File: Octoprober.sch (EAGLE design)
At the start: 98 parts, among them J1 10118193-0001LF, P1 TC33X-1, SW1 EVQ-Q2203W, SW2 EVQ-Q2203W, SW3 EVQ-Q2203W, SW4 EVQ-Q2203W, SW5 EVQ-Q2203W, U1 P8X32A-M44, U10 MAX31855KASA+, U11 MAX31855KASA+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

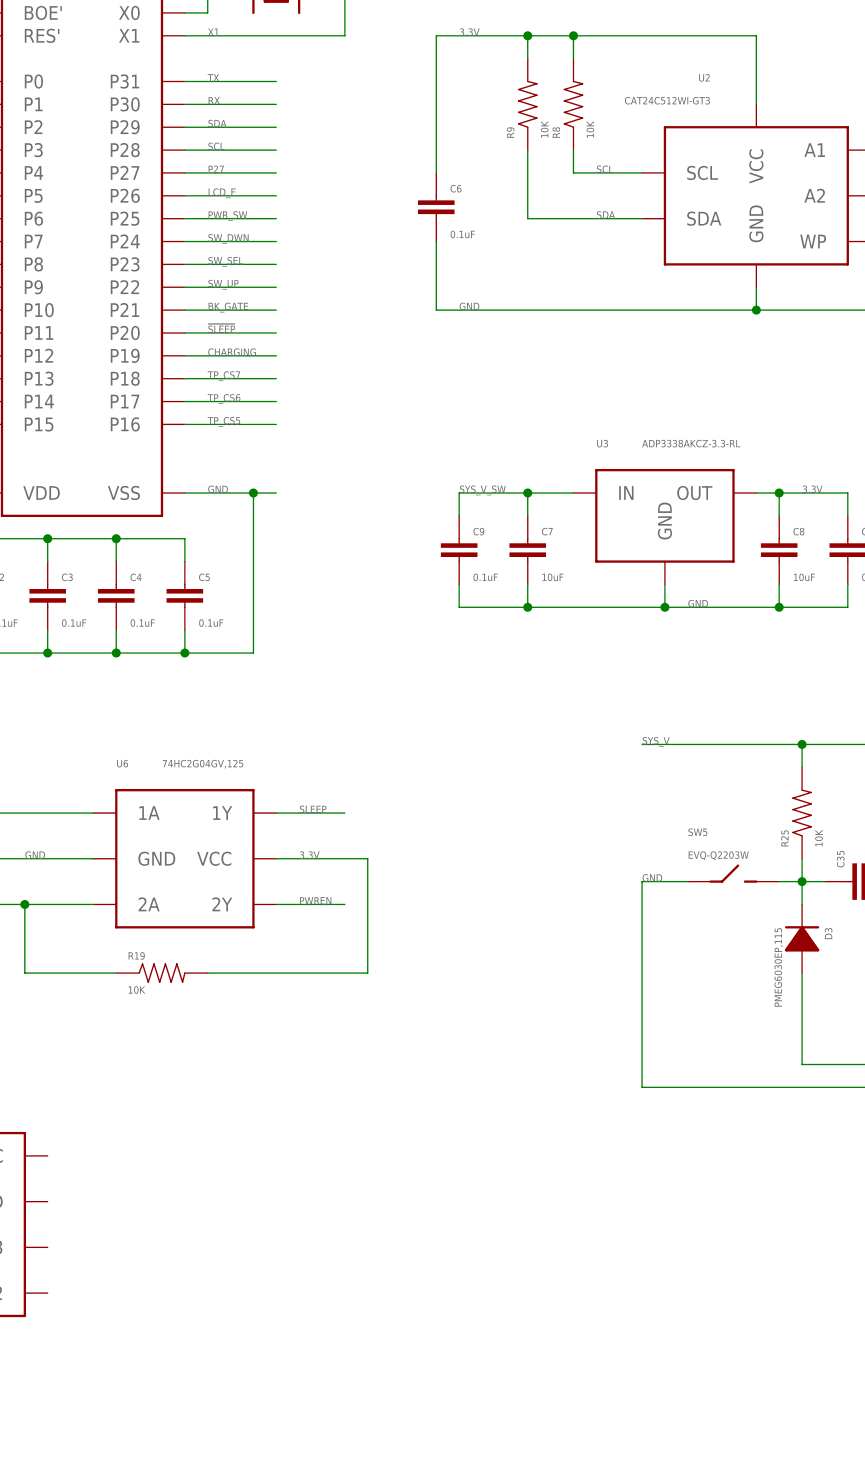
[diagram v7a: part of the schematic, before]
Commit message: Add optocouple.
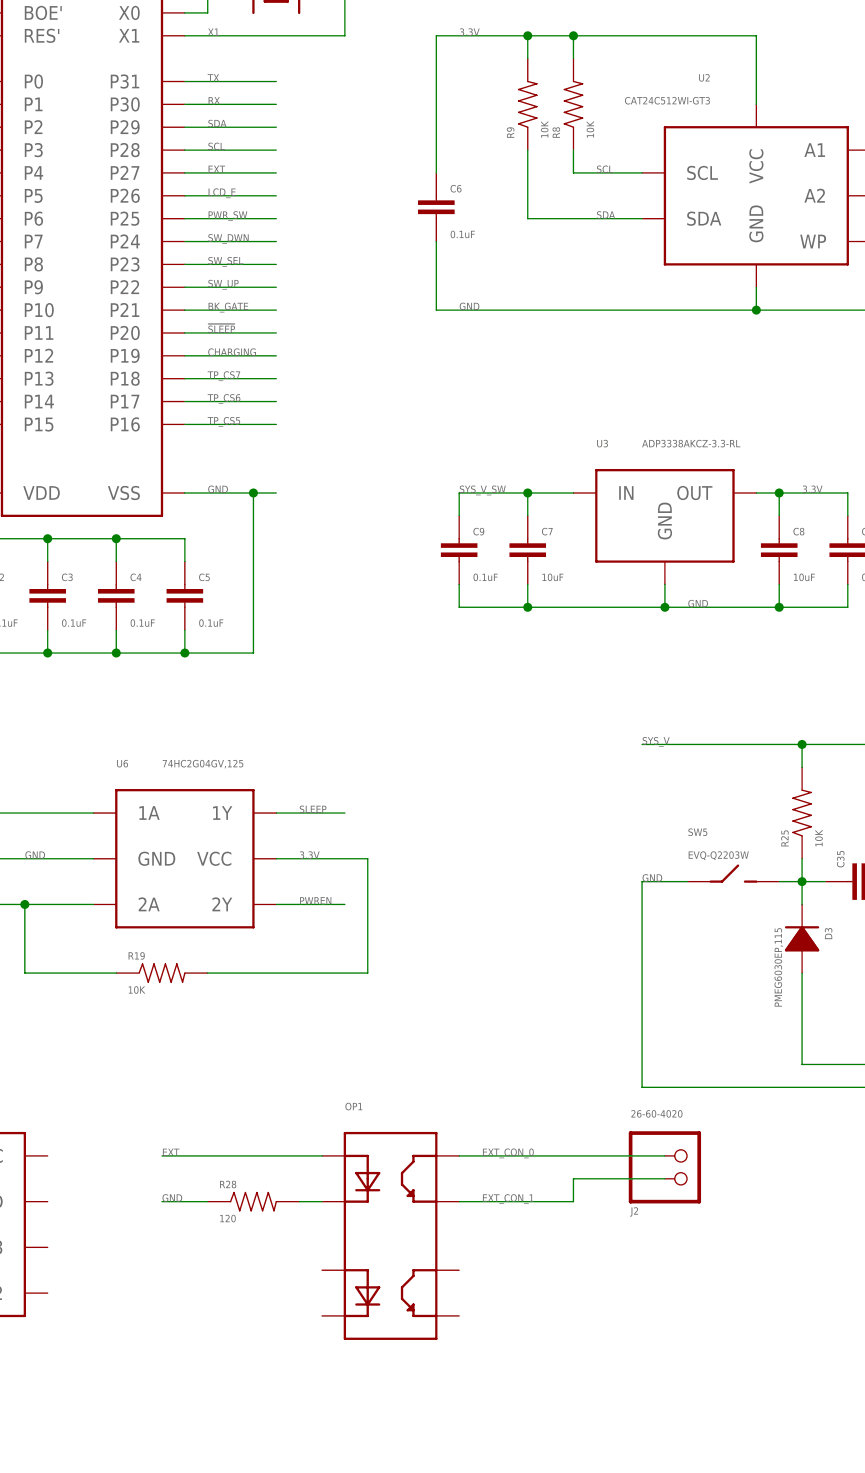
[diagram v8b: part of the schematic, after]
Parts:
- added J2: 26-60-4020, PP_Connectors:PH_1X02MOLEX_26-61-4020
- added OP1: (no value), PP_DigitalIC:ACPL-227SOIC-8
- added R28: 120, PP_Passives:RESISTOR0402
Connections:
- removed net P27: U1.P27
- new net EXT: OP1.1, U1.P27
- new net EXT_CON_0: J2.2, OP1.8
- new net EXT_CON_1: J2.1, OP1.7
- new net N$6: OP1.2, R28.2
- net GND: now also R28.1
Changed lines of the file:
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@@
 <?xml version="1.0" encoding="utf-8"?>
 <!DOCTYPE eagle SYSTEM "eagle.dtd">
-<eagle version="6.3">
+<eagle version="6.5.0">
 <drawing>
 <settings>
@@
 <grid distance="0.1" unitdist="inch" unit="inch" style="lines" multiple="1" display="no" altdistance="0.01" altunitdist="inch" altunit="inch"/>
 <layers>
-<layer number="1" name="Top" color="4" fill="1" visible="yes" active="no"/>
-<layer number="16" name="Bottom" color="1" fill="1" visible="yes" active="no"/>
-<layer number="17" name="Pads" color="2" fill="1" visible="yes" active="no"/>
-<layer number="18" name="Vias" color="2" fill="1" visible="yes" active="no"/>
-<layer number="19" name="Unrouted" color="6" fill="1" visible="yes" active="no"/>
-<layer number="20" name="Dimension" color="15" fill="1" visible="yes" active="no"/>
-<layer number="21" name="tPlace" color="7" fill="1" visible="yes" active="no"/>
-<layer number="22" name="bPlace" color="7" fill="1" visible="yes" active="no"/>
-<layer number="23" name="tOrigins" color="15" fill="1" visible="yes" active="no"/>
-<layer number="24" name="bOrigins" color="15" fill="1" visible="yes" active="no"/>
-<layer number="25" name="tNames" color="7" fill="1" visible="yes" active="no"/>
-<layer number="26" name="bNames" color="7" fill="1" visible="yes" active="no"/>
-<layer number="27" name="tValues" color="7" fill="1" visible="yes" active="no"/>
-<layer number="28" name="bValues" color="7" fill="1" visible="yes" active="no"/>
+<layer number="1" name="Top" color="4" fill="1" visible="no" active="no"/>
+<layer number="16" name="Bottom" color="1" fill="1" visible="no" active="no"/>
+<layer number="17" name="Pads" color="2" fill="1" visible="no" active="no"/>
+<layer number="18" name="Vias" color="2" fill="1" visible="no" active="no"/>
+<layer number="19" name="Unrouted" color="6" fill="1" visible="no" active="no"/>
+<layer number="20" name="Dimension" color="15" fill="1" visible="no" active="no"/>
+<layer number="21" name="tPlace" color="7" fill="1" visible="no" active="no"/>
+<layer number="22" name="bPlace" color="7" fill="1" visible="no" active="no"/>
+<layer number="23" name="tOrigins" color="15" fill="1" visible="no" active="no"/>
+<layer number="24" name="bOrigins" color="15" fill="1" visible="no" active="no"/>
+<layer number="25" name="tNames" color="7" fill="1" visible="no" active="no"/>
+<layer number="26" name="bNames" color="7" fill="1" visible="no" active="no"/>
+<layer number="27" name="tValues" color="7" fill="1" visible="no" active="no"/>
+<layer number="28" name="bValues" color="7" fill="1" visible="no" active="no"/>
 <layer number="29" name="tStop" color="7" fill="3" visible="no" active="no"/>
 <layer number="30" name="bStop" color="7" fill="6" visible="no" active="no"/>
@@
 <layer number="35" name="tGlue" color="7" fill="4" visible="no" active="no"/>
 <layer number="36" name="bGlue" color="7" fill="5" visible="no" active="no"/>
-<layer number="37" name="tTest" color="7" fill="1" visible="yes" active="no"/>
-<layer number="38" name="bTest" color="7" fill="1" visible="yes" active="no"/>
+<layer number="37" name="tTest" color="7" fill="1" visible="no" active="no"/>
+<layer number="38" name="bTest" color="7" fill="1" visible="no" active="no"/>
 <layer number="39" name="tKeepout" color="4" fill="11" visible="no" active="no"/>
 <layer number="40" name="bKeepout" color="1" fill="11" visible="no" active="no"/>
@@
 <layer number="44" name="Drills" color="7" fill="1" visible="no" active="no"/>
 <layer number="45" name="Holes" color="7" fill="1" visible="no" active="no"/>
-<layer number="46" name="Milling" color="3" fill="1" visible="yes" active="no"/>
-<layer number="47" name="Measures" color="7" fill="1" visible="yes" active="no"/>
-<layer number="48" name="Document" color="7" fill="1" visible="yes" active="no"/>
-<layer number="49" name="Reference" color="7" fill="1" visible="yes" active="no"/>
-<layer number="50" name="dxf" color="7" fill="1" visible="yes" active="no"/>
-<layer number="51" name="tDocu" color="7" fill="1" visible="yes" active="no"/>
-<layer number="52" name="bDocu" color="7" fill="1" visible="yes" active="no"/>
-<layer number="53" name="tGND_GNDA" color="7" fill="9" visible="yes" active="no"/>
-<layer number="54" name="bGND_GNDA" color="1" fill="9" visible="yes" active="no"/>
-<layer number="56" name="wert" color="7" fill="1" visible="yes" active="no"/>
+<layer number="46" name="Milling" color="3" fill="1" visible="no" active="no"/>
+<layer number="47" name="Measures" color="7" fill="1" visible="no" active="no"/>
+<layer number="48" name="Document" color="7" fill="1" visible="no" active="no"/>
+<layer number="49" name="Reference" color="7" fill="1" visible="no" active="no"/>
+<layer number="50" name="dxf" color="7" fill="1" visible="no" active="no"/>
+<layer number="51" name="tDocu" color="7" fill="1" visible="no" active="no"/>
+<layer number="52" name="bDocu" color="7" fill="1" visible="no" active="no"/>
+<layer number="53" name="tGND_GNDA" color="7" fill="9" visible="no" active="no"/>
+<layer number="54" name="bGND_GNDA" color="1" fill="9" visible="no" active="no"/>
+<layer number="56" name="wert" color="7" fill="1" visible="no" active="no"/>
 <layer number="91" name="Nets" color="2" fill="1" visible="yes" active="yes"/>
 <layer number="92" name="Busses" color="1" fill="1" visible="yes" active="yes"/>
@@
 <part name="U18" library="PP_DigitalIC" deviceset="AD799X" device="SOT-23-8" value="AD7999YRJZ-1500RL7"/>
 <part name="U$2" library="PP_Aesthetics" deviceset="OCTOPROBER_LOGO" device="NORMAL"/>
+<part name="J2" library="PP_Connectors" deviceset="PH_1X02" device="MOLEX_26-61-4020" value="26-60-4020"/>
+<part name="OP1" library="PP_DigitalIC" deviceset="ACPL-227" device="SOIC-8"/>
+<part name="R28" library="PP_Passives" deviceset="RESISTOR" device="0402" value="120"/>
 </parts>
 <sheets>
@@
 <instance part="U18" gate="G$1" x="-15.24" y="-101.6"/>
 <instance part="U$2" gate="G$1" x="-284.48" y="-101.6"/>
+<instance part="J2" gate="G$1" x="63.5" y="-99.06" rot="MR180"/>
+<instance part="OP1" gate="G$1" x="33.02" y="-104.14"/>
+<instance part="R28" gate="G$1" x="17.78" y="-101.6"/>
 </instances>
 <busses>
@@
 </segment>
 </net>
-<net name="P27" class="0">
+<net name="EXT" class="0">
 <segment>
 <pinref part="U1" gate="G$1" pin="P27"/>
 <wire x1="10.16" y1="12.7" x2="20.32" y2="12.7" width="0.1524" layer="91"/>
 <label x="12.7" y="12.7" size="0.8128" layer="95" font="vector"/>
+</segment>
+<segment>
+<pinref part="OP1" gate="G$1" pin="1"/>
+<wire x1="25.4" y1="-96.52" x2="7.62" y2="-96.52" width="0.1524" layer="91"/>
+<label x="7.62" y="-96.52" size="0.8128" layer="95" font="vector"/>
 </segment>
 </net>
@@
 <wire x1="109.22" y1="-88.9" x2="60.96" y2="-88.9" width="0.1524" layer="91"/>
 <wire x1="60.96" y1="-88.9" x2="60.96" y2="-66.04" width="0.1524" layer="91"/>
+</segment>
+<segment>
+<pinref part="R28" gate="G$1" pin="1"/>
+<wire x1="12.7" y1="-101.6" x2="7.62" y2="-101.6" width="0.1524" layer="91"/>
+<label x="7.62" y="-101.6" size="0.8128" layer="95" font="vector"/>
 </segment>
 </net>
@@
 </segment>
 </net>
+<net name="N$6" class="0">
+<segment>
+<pinref part="OP1" gate="G$1" pin="2"/>
+<pinref part="R28" gate="G$1" pin="2"/>
+<wire x1="25.4" y1="-101.6" x2="22.86" y2="-101.6" width="0.1524" layer="91"/>
+</segment>
+</net>
+<net name="EXT_CON_1" class="0">
+<segment>
+<pinref part="OP1" gate="G$1" pin="7"/>
+<wire x1="40.64" y1="-101.6" x2="53.34" y2="-101.6" width="0.1524" layer="91"/>
+<label x="43.18" y="-101.6" size="0.8128" layer="95" font="vector"/>
+<wire x1="53.34" y1="-99.06" x2="53.34" y2="-101.6" width="0.1524" layer="91"/>
+<pinref part="J2" gate="G$1" pin="1"/>
+<wire x1="63.5" y1="-99.06" x2="53.34" y2="-99.06" width="0.1524" layer="91"/>
+</segment>
+</net>
+<net name="EXT_CON_0" class="0">
+<segment>
+<pinref part="OP1" gate="G$1" pin="8"/>
+<label x="43.18" y="-96.52" size="0.8128" layer="95" font="vector"/>
+<wire x1="40.64" y1="-96.52" x2="63.5" y2="-96.52" width="0.1524" layer="91"/>
+<pinref part="J2" gate="G$1" pin="2"/>
+</segment>
+</net>
